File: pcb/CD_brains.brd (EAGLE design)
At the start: 67.3 x 80.3 mm, 21 parts, among them SW2 ROTARTY_ENCODER, U1 TC4422AVOA, U2 LCD-16X2SILK

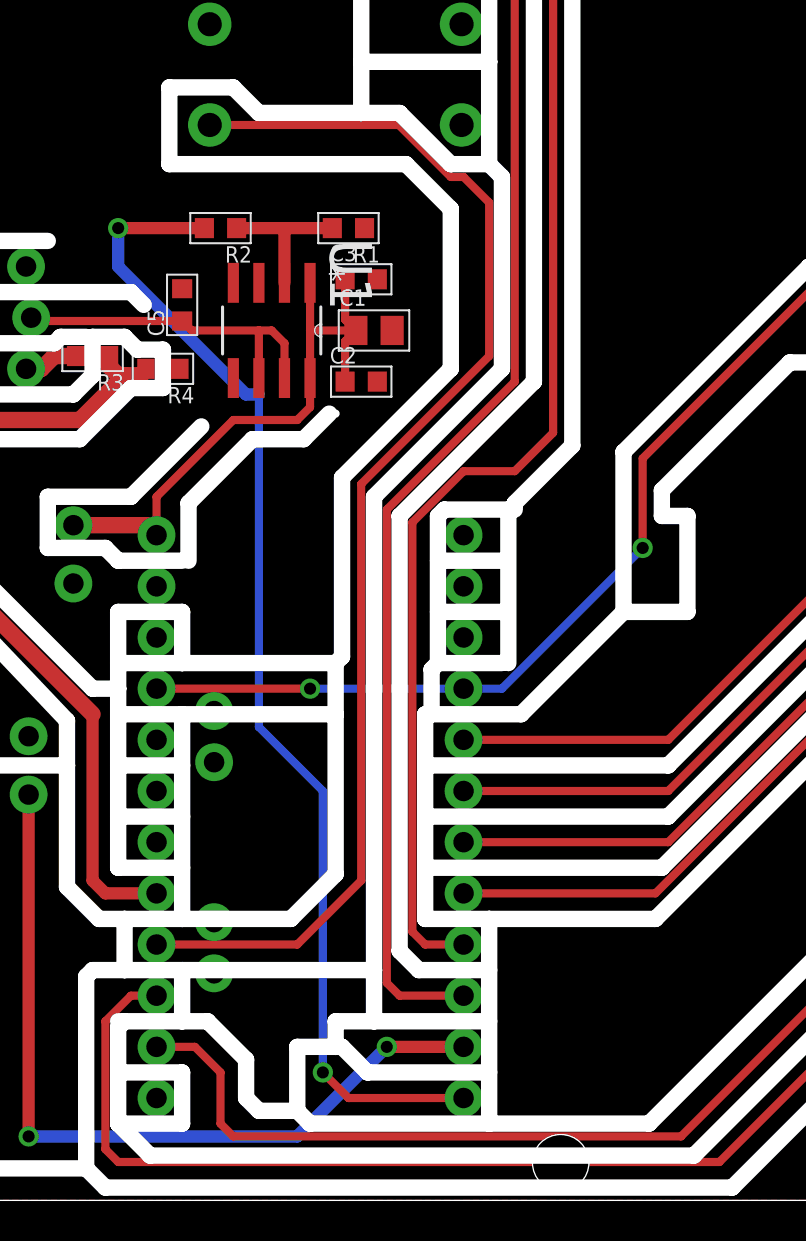
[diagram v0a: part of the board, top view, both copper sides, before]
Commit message: fixed CD BRAINS Inconsistencies
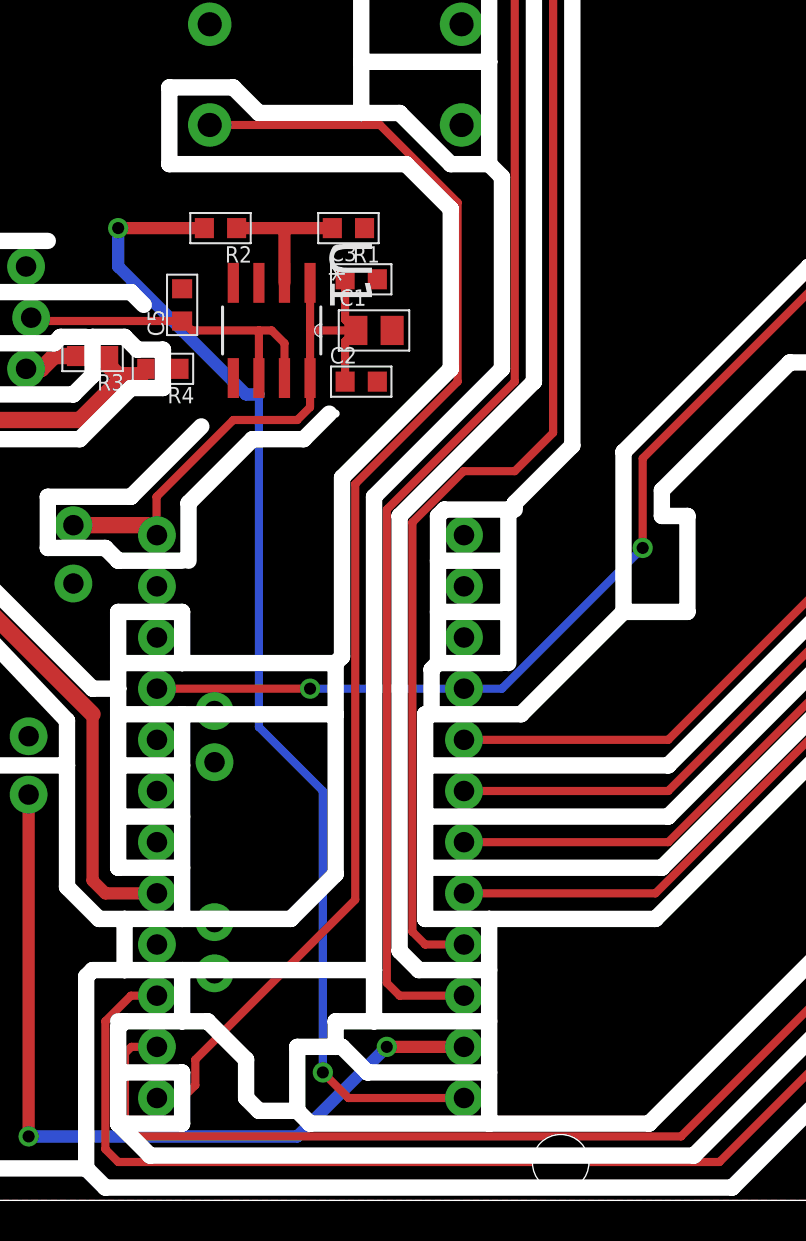
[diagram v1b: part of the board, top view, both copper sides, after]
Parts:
- removed ARDUINO: ARDUINO_PRO_MINI, _my-parts:ARDUINO_PRO_MINI
- added U$1: ARDUINO_PRO_MINI, _my-parts:ARDUINO_PRO_MINI
- R35: value 1k -> DNP
- R36: value 1k -> 0k
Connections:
- removed net MISO: ARDUINO.15, U2.4
- removed net MOSI: ARDUINO.14, U2.6
- removed net UI_SW*: ARDUINO.13
- new net D11: U$1.14, U2.6
- new net D12: U$1.15, U2.4
- net 5V: now also U$1.21; no longer ARDUINO.21
- net 9V: now also U$1.24; no longer ARDUINO.24
- net CAP_V_IN: now also U$1.17; no longer ARDUINO.17
- net D2: now also U$1.5; no longer ARDUINO.5
- net D3: now also U$1.6; no longer ARDUINO.6
- net D4: now also U$1.7; no longer ARDUINO.7
- net D5: now also U$1.8; no longer ARDUINO.8
- net ENC_01: now also U$1.9; no longer ARDUINO.9
- net ENC_02: now also U$1.10; no longer ARDUINO.10
- net FT_SW: now also U$1.11; no longer ARDUINO.11
- net GND: now also U$1.23, U$1.4; no longer ARDUINO.23, ARDUINO.4
- net TRIG: now also U$1.12; no longer ARDUINO.12
- net UI_SW: now also U$1.13; no longer ARDUINO.16
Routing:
- net D12: track 0.00 -> 68.7 mm
- net MISO: track 68.7 -> 0.00 mm
- net D11: track 0.00 -> 65.1 mm
- net MOSI: track 61.4 -> 0.00 mm
- net UI_SW: track 63.2 -> 65.3 mm
